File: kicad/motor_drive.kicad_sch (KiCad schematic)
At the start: 10 parts, among them U6 DRV8452DDWR

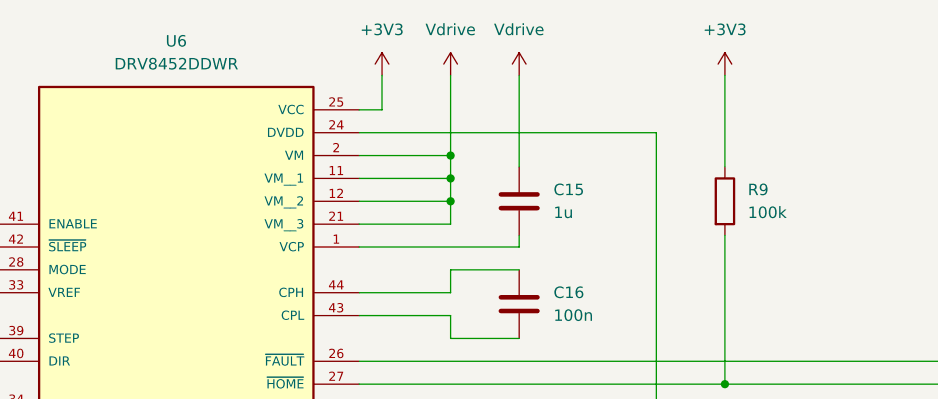
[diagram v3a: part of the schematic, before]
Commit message: Finished the schematic and started the PCB.
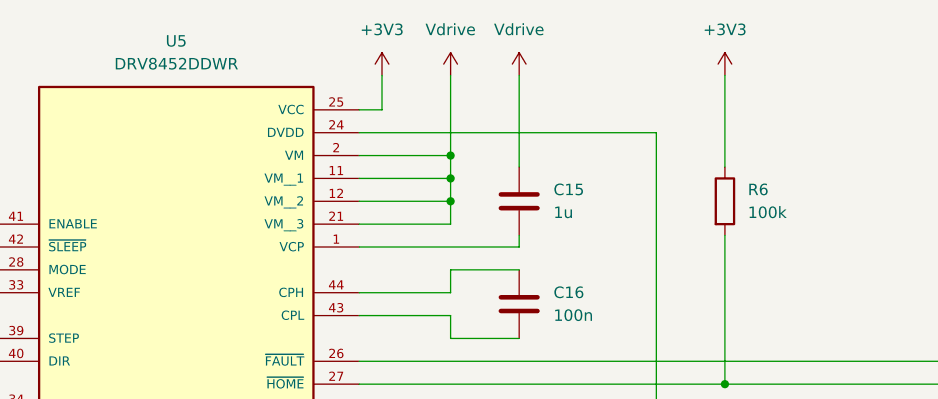
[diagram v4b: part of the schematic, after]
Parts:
- R6: renamed from R9; MF YAGEO -> Yageo
- renumbered U6 to U5
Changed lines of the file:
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@@
 		(dnp no)
 		(fields_autoplaced yes)
-		(property "Reference" "#PWR052"
+		(property "Reference" "#PWR046"
 			(at 160.02 157.48 0)
 			(effects
@@
 			(project ""
 				(path "/914c4b67-a7a4-47f3-8515-668040fd3f8c/e5516eed-629d-4c0b-bb03-2e43d030d802"
-					(reference "#PWR052")
+					(reference "#PWR046")
 					(unit 1)
 				)
@@
 		(dnp no)
 		(fields_autoplaced yes)
-		(property "Reference" "#PWR057"
+		(property "Reference" "#PWR051"
 			(at 231.14 157.48 0)
 			(effects
@@
 			(project "tv_slider"
 				(path "/914c4b67-a7a4-47f3-8515-668040fd3f8c/e5516eed-629d-4c0b-bb03-2e43d030d802"
-					(reference "#PWR057")
+					(reference "#PWR051")
 					(unit 1)
 				)
@@
 		(on_board yes)
 		(dnp no)
-		(property "Reference" "#PWR044"
+		(property "Reference" "#PWR038"
 			(at 175.26 50.8 0)
 			(effects
@@
 			(project "tv_slider"
 				(path "/914c4b67-a7a4-47f3-8515-668040fd3f8c/e5516eed-629d-4c0b-bb03-2e43d030d802"
-					(reference "#PWR044")
+					(reference "#PWR038")
 					(unit 1)
 				)
@@
 		(dnp no)
 		(fields_autoplaced yes)
-		(property "Reference" "#PWR041"
+		(property "Reference" "#PWR035"
 			(at 111.76 50.8 0)
 			(effects
@@
 			(project "tv_slider"
 				(path "/914c4b67-a7a4-47f3-8515-668040fd3f8c/e5516eed-629d-4c0b-bb03-2e43d030d802"
-					(reference "#PWR041")
+					(reference "#PWR035")
 					(unit 1)
 				)
@@
 		(dnp no)
 		(fields_autoplaced yes)
-		(property "Reference" "#PWR051"
+		(property "Reference" "#PWR045"
 			(at 111.76 157.48 0)
 			(effects
@@
 			(project "tv_slider"
 				(path "/914c4b67-a7a4-47f3-8515-668040fd3f8c/e5516eed-629d-4c0b-bb03-2e43d030d802"
-					(reference "#PWR051")
+					(reference "#PWR045")
 					(unit 1)
 				)
@@
 		(on_board yes)
 		(dnp no)
-		(property "Reference" "#PWR047"
+		(property "Reference" "#PWR041"
 			(at 204.47 142.24 0)
 			(effects
@@
 			(project "tv_slider"
 				(path "/914c4b67-a7a4-47f3-8515-668040fd3f8c/e5516eed-629d-4c0b-bb03-2e43d030d802"
-					(reference "#PWR047")
+					(reference "#PWR041")
 					(unit 1)
 				)
@@
 		(dnp no)
 		(fields_autoplaced yes)
-		(property "Reference" "R9"
+		(property "Reference" "R6"
 			(at 200.66 59.6899 0)
 			(effects
@@
 			)
 		)
-		(property "MF" "YAGEO"
+		(property "MF" "Yageo"
 			(at 198.12 60.96 0)
 			(effects
@@
 			(project "tv_slider"
 				(path "/914c4b67-a7a4-47f3-8515-668040fd3f8c/e5516eed-629d-4c0b-bb03-2e43d030d802"
-					(reference "R9")
+					(reference "R6")
 					(unit 1)
 				)
@@
 		(dnp no)
 		(fields_autoplaced yes)
-		(property "Reference" "#PWR055"
+		(property "Reference" "#PWR049"
 			(at 204.47 157.48 0)
 			(effects
@@
 			(project "tv_slider"
 				(path "/914c4b67-a7a4-47f3-8515-668040fd3f8c/e5516eed-629d-4c0b-bb03-2e43d030d802"
-					(reference "#PWR055")
+					(reference "#PWR049")
 					(unit 1)
 				)
@@
 		(dnp no)
 		(fields_autoplaced yes)
-		(property "Reference" "#PWR053"
+		(property "Reference" "#PWR047"
 			(at 175.26 157.48 0)
 			(effects
@@
 			(project "tv_slider"
 				(path "/914c4b67-a7a4-47f3-8515-668040fd3f8c/e5516eed-629d-4c0b-bb03-2e43d030d802"
-					(reference "#PWR053")
+					(reference "#PWR047")
 					(unit 1)
 				)
@@
 		(dnp no)
 		(fields_autoplaced yes)
-		(property "Reference" "#PWR042"
+		(property "Reference" "#PWR036"
 			(at 160.02 50.8 0)
 			(effects
@@
 			(project ""
 				(path "/914c4b67-a7a4-47f3-8515-668040fd3f8c/e5516eed-629d-4c0b-bb03-2e43d030d802"
-					(reference "#PWR042")
+					(reference "#PWR036")
 					(unit 1)
 				)
@@
 		(on_board yes)
 		(dnp no)
-		(property "Reference" "#PWR049"
+		(property "Reference" "#PWR043"
 			(at 231.14 142.24 0)
 			(effects
@@
 			(project "tv_slider"
 				(path "/914c4b67-a7a4-47f3-8515-668040fd3f8c/e5516eed-629d-4c0b-bb03-2e43d030d802"
-					(reference "#PWR049")
+					(reference "#PWR043")
 					(unit 1)
 				)
@@
 		(on_board yes)
 		(dnp no)
-		(property "Reference" "#PWR048"
+		(property "Reference" "#PWR042"
 			(at 217.17 142.24 0)
 			(effects
@@
 			(project "tv_slider"
 				(path "/914c4b67-a7a4-47f3-8515-668040fd3f8c/e5516eed-629d-4c0b-bb03-2e43d030d802"
-					(reference "#PWR048")
+					(reference "#PWR042")
 					(unit 1)
 				)
@@
 		(on_board yes)
 		(dnp no)
-		(property "Reference" "#PWR050"
+		(property "Reference" "#PWR044"
 			(at 245.11 142.24 0)
 			(effects
@@
 			(project "tv_slider"
 				(path "/914c4b67-a7a4-47f3-8515-668040fd3f8c/e5516eed-629d-4c0b-bb03-2e43d030d802"
-					(reference "#PWR050")
+					(reference "#PWR044")
 					(unit 1)
 				)
@@
 		(dnp no)
 		(fields_autoplaced yes)
-		(property "Reference" "#PWR045"
+		(property "Reference" "#PWR039"
 			(at 198.12 50.8 0)
 			(effects
@@
 			(project "tv_slider"
 				(path "/914c4b67-a7a4-47f3-8515-668040fd3f8c/e5516eed-629d-4c0b-bb03-2e43d030d802"
-					(reference "#PWR045")
+					(reference "#PWR039")
 					(unit 1)
 				)
@@
 		(dnp no)
 		(fields_autoplaced yes)
-		(property "Reference" "#PWR056"
+		(property "Reference" "#PWR050"
 			(at 217.17 157.48 0)
 			(effects
@@
 			(project "tv_slider"
 				(path "/914c4b67-a7a4-47f3-8515-668040fd3f8c/e5516eed-629d-4c0b-bb03-2e43d030d802"
-					(reference "#PWR056")
+					(reference "#PWR050")
 					(unit 1)
 				)
@@
 		(dnp no)
 		(fields_autoplaced yes)
-		(property "Reference" "#PWR054"
+		(property "Reference" "#PWR048"
 			(at 190.5 157.48 0)
 			(effects
@@
 			(project "tv_slider"
 				(path "/914c4b67-a7a4-47f3-8515-668040fd3f8c/e5516eed-629d-4c0b-bb03-2e43d030d802"
-					(reference "#PWR054")
+					(reference "#PWR048")
 					(unit 1)
 				)
@@
 		(on_board yes)
 		(dnp no)
-		(property "Reference" "#PWR043"
+		(property "Reference" "#PWR037"
 			(at 167.64 50.8 0)
 			(effects
@@
 			(project ""
 				(path "/914c4b67-a7a4-47f3-8515-668040fd3f8c/e5516eed-629d-4c0b-bb03-2e43d030d802"
-					(reference "#PWR043")
+					(reference "#PWR037")
 					(unit 1)
 				)
@@
 		(dnp no)
 		(fields_autoplaced yes)
-		(property "Reference" "#PWR046"
+		(property "Reference" "#PWR040"
 			(at 175.26 142.24 0)
 			(effects
@@
 			(project "tv_slider"
 				(path "/914c4b67-a7a4-47f3-8515-668040fd3f8c/e5516eed-629d-4c0b-bb03-2e43d030d802"
-					(reference "#PWR046")
+					(reference "#PWR040")
 					(unit 1)
 				)
@@
 		(dnp no)
 		(fields_autoplaced yes)
-		(property "Reference" "#PWR058"
+		(property "Reference" "#PWR052"
 			(at 245.11 157.48 0)
 			(effects
@@
 			(project "tv_slider"
 				(path "/914c4b67-a7a4-47f3-8515-668040fd3f8c/e5516eed-629d-4c0b-bb03-2e43d030d802"
-					(reference "#PWR058")
+					(reference "#PWR052")
 					(unit 1)
 				)
@@
 		(dnp no)
 		(fields_autoplaced yes)
-		(property "Reference" "U6"
+		(property "Reference" "U5"
 			(at 137.16 43.18 0)
 			(effects
@@
 			(project "tv_slider"
 				(path "/914c4b67-a7a4-47f3-8515-668040fd3f8c/e5516eed-629d-4c0b-bb03-2e43d030d802"
-					(reference "U6")
-					(unit 1)
-				)
+					(reference "U5")
+					(unit 1)
+				)

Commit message: Completed the PCB design. Ready for final review.
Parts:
- removed R6: 100k, Resistor_SMD:R_0603_1608Metric, symbol Device:R
- removed U5: DRV8452DDWR, local_library:IC_DRV8452DDWR, symbol local_library:DRV8452DDWR
- added U9: DRV8452SPWPR, local_library:IC_DRV8452SPWPR, symbol local_library:DRV8452SPWPR
- C21, C22: value 150u -> 100u; footprint Capacitor_SMD:CP_Elec_10x12.5 -> Capacitor_SMD:CP_Elec_8x11.9; MP A768MS157M1HLAE024 -> A768KS107M1HLAE030; SupplierPN 399-A768MS157M1HLAE024TR-ND -> 399-A768KS107M1HLAE030CT-ND
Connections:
- net +3V3: now also U9.19 (VCC)
- net A+: now also U9.4 (AOUT1), U9.5 (AOUT1__1)
- net A-: now also U9.6 (AOUT2), U9.7 (AOUT2__1)
- net B+: now also U9.10 (BOUT1), U9.11 (BOUT1__1)
- net B-: now also U9.8 (BOUT2), U9.9 (BOUT2__1)
- net DIR: now also U9.24 (DIR)
- net ENABLE: now also U9.25 (ENABLE)
- net GND: now also U9.12 (PGNDB), U9.14 (GND), U9.17 (VREF), U9.29 (PAD), U9.3 (PGNDA)
- net MISO: now also U9.20 (SDO)
- net MOSI: now also U9.21 (SDI)
- net SCLK: now also U9.22 (SCLK)
- net STEP: now also U9.23 (STEP)
- net Vdrive: now also U9.13 (VM__1), U9.2 (VM)
- net ~{CS}: now also U9.18 (~{SCS})
- net ~{FAULT}: now also U9.16 (~{FAULT})
- net ~{SLEEP}: now also U9.26 (~{SLEEP})
- net at C15.2: now also U9.1 (VCP)
- net at C18.1: now also U9.15 (DVDD)
- net at C16.2: now also U9.27 (CPL)
- net at C16.1: now also U9.28 (CPH)
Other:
- moved on the sheet: C15, C16, C17, C18, C19, C20, C22

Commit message: Reviewed the part numbers, footprints and pin numbers.
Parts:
- C21, C22: Dielectric Electrolytic -> (none)
- U9: MF (none) -> Texas Instruments; MP (none) -> DRV8452SPWPR; Supplier (none) -> Digi-Key; SupplierPN (none) -> 296-DRV8452SPWPRCT-ND
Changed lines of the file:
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@@
+			)
+		)
+		(property "MF" "Texas Instruments"
+			(at 137.16 73.66 0)
+			(effects
+				(font
+					(size 1.27 1.27)
+				)
+				(hide yes)
+			)
+		)
+		(property "MP" "DRV8452SPWPR"
+			(at 137.16 73.66 0)
+			(effects
+				(font
+					(size 1.27 1.27)
+				)
+				(hide yes)
+			)
+		)
+		(property "SNAPEDA_PN" ""
+			(at 137.16 73.66 0)
+			(effects
+				(font
+					(size 1.27 1.27)
+				)
+				(hide yes)
+			)
+		)
+		(property "Supplier" "Digi-Key"
+			(at 137.16 73.66 0)
+			(effects
+				(font
+					(size 1.27 1.27)
+				)
+				(hide yes)
+			)
+		)
+		(property "SupplierPN" "296-DRV8452SPWPRCT-ND"
+			(at 137.16 73.66 0)
+			(effects
+				(font
+					(size 1.27 1.27)
+				)
+				(hide yes)
 			)
 		)
@@
 			)
 		)
-		(property "Dielectric" "Electrolytic"
+		(property "Dielectric" ""
 			(at 232.41 116.84 0)
 			(effects
@@
 		)
 		(property "SupplierPN" "399-A768KS107M1HLAE030CT-ND"
+			(at 232.41 116.84 0)
+			(effects
+				(font
+					(size 1.27 1.27)
+				)
+				(hide yes)
+			)
+		)
+		(property "SNAPEDA_PN" ""
 			(at 232.41 116.84 0)
 			(effects
@@
 			)
 		)
+		(property "SNAPEDA_PN" ""
+			(at 175.26 50.8 0)
+			(effects
+				(font
+					(size 1.27 1.27)
+				)
+				(hide yes)
+			)
+		)
 		(pin "2"
 		)
@@
 		)
 		(property "SupplierPN" "490-3285-1-ND"
+			(at 176.53 116.84 0)
+			(effects
+				(font
+					(size 1.27 1.27)
+				)
+				(hide yes)
+			)
+		)
+		(property "SNAPEDA_PN" ""
 			(at 176.53 116.84 0)
 			(effects
@@
 			)
 		)
+		(property "SNAPEDA_PN" ""
+			(at 191.77 116.84 0)
+			(effects
+				(font
+					(size 1.27 1.27)
+				)
+				(hide yes)
+			)
+		)
 		(pin "2"
 		)
@@
 			)
 		)
+		(property "SNAPEDA_PN" ""
+			(at 205.74 116.84 0)
+			(effects
+				(font
+					(size 1.27 1.27)
+				)
+				(hide yes)
+			)
+		)
 		(pin "2"
 		)
@@
 			)
 		)
+		(property "SNAPEDA_PN" ""
+			(at 218.44 116.84 0)
+			(effects
+				(font
+					(size 1.27 1.27)
+				)
+				(hide yes)
+			)
+		)
 		(pin "2"
 		)
@@
 			)
 		)
-		(property "Dielectric" "Electrolytic"
+		(property "Dielectric" ""
 			(at 246.38 116.84 0)
 			(effects
@@
 		)
 		(property "SupplierPN" "399-A768KS107M1HLAE030CT-ND"
+			(at 246.38 116.84 0)
+			(effects
+				(font
+					(size 1.27 1.27)
+				)
+				(hide yes)
+			)
+		)
+		(property "SNAPEDA_PN" ""
 			(at 246.38 116.84 0)
 			(effects
@@
 			(at 175.26 62.23 0)
 			(effects
+				(font
+					(size 1.27 1.27)
+				)
+				(hide yes)
+			)
+		)
+		(property "SNAPEDA_PN" ""
+			(at 175.26 62.23 0)
+			(effects

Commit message: Re-annotated and added extra capacitors for the 5V and 3V3 DC-DC converters. Added testpoints to the electronic fuse.
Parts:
- renumbered C15 to C17, C16 to C18, C17 to C19, C18 to C20, C19 to C21, C20 to C22, C21 to C23, C22 to C24, U9 to U5
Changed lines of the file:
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@@
 		(dnp no)
 		(fields_autoplaced yes)
-		(property "Reference" "U9"
+		(property "Reference" "U5"
 			(at 137.16 38.1 0)
 			(effects
@@
 			(project ""
 				(path "/914c4b67-a7a4-47f3-8515-668040fd3f8c/e5516eed-629d-4c0b-bb03-2e43d030d802"
-					(reference "U9")
+					(reference "U5")
 					(unit 1)
 				)
@@
 		(dnp no)
 		(fields_autoplaced yes)
-		(property "Reference" "#PWR046"
+		(property "Reference" "#PWR048"
 			(at 161.29 129.54 0)
 			(effects
@@
 			(project ""
 				(path "/914c4b67-a7a4-47f3-8515-668040fd3f8c/e5516eed-629d-4c0b-bb03-2e43d030d802"
-					(reference "#PWR046")
+					(reference "#PWR048")
 					(unit 1)
 				)
@@
 		(dnp no)
 		(fields_autoplaced yes)
-		(property "Reference" "#PWR051"
+		(property "Reference" "#PWR053"
 			(at 232.41 129.54 0)
 			(effects
@@
 			(project "tv_slider"
 				(path "/914c4b67-a7a4-47f3-8515-668040fd3f8c/e5516eed-629d-4c0b-bb03-2e43d030d802"
-					(reference "#PWR051")
+					(reference "#PWR053")
 					(unit 1)
 				)
@@
 		(dnp no)
 		(fields_autoplaced yes)
-		(property "Reference" "C21"
+		(property "Reference" "C23"
 			(at 236.22 114.6809 0)
 			(effects
@@
 			(project "tv_slider"
 				(path "/914c4b67-a7a4-47f3-8515-668040fd3f8c/e5516eed-629d-4c0b-bb03-2e43d030d802"
-					(reference "C21")
+					(reference "C23")
 					(unit 1)
 				)
@@
 		(on_board yes)
 		(dnp no)
-		(property "Reference" "#PWR038"
+		(property "Reference" "#PWR041"
 			(at 175.26 44.45 0)
 			(effects
@@
 			(project "tv_slider"
 				(path "/914c4b67-a7a4-47f3-8515-668040fd3f8c/e5516eed-629d-4c0b-bb03-2e43d030d802"
-					(reference "#PWR038")
+					(reference "#PWR041")
 					(unit 1)
 				)
@@
 		(dnp no)
 		(fields_autoplaced yes)
-		(property "Reference" "#PWR045"
+		(property "Reference" "#PWR047"
 			(at 113.03 129.54 0)
 			(effects
@@
 			(project "tv_slider"
 				(path "/914c4b67-a7a4-47f3-8515-668040fd3f8c/e5516eed-629d-4c0b-bb03-2e43d030d802"
-					(reference "#PWR045")
+					(reference "#PWR047")
 					(unit 1)
 				)
@@
 		(on_board yes)
 		(dnp no)
-		(property "Reference" "#PWR041"
+		(property "Reference" "#PWR043"
 			(at 205.74 114.3 0)
 			(effects
@@
 			(project "tv_slider"
 				(path "/914c4b67-a7a4-47f3-8515-668040fd3f8c/e5516eed-629d-4c0b-bb03-2e43d030d802"
-					(reference "#PWR041")
+					(reference "#PWR043")
 					(unit 1)
 				)
@@
 		(dnp no)
 		(fields_autoplaced yes)
-		(property "Reference" "C15"
+		(property "Reference" "C17"
 			(at 179.07 49.5299 0)
 			(effects
@@
 			(project "tv_slider"
 				(path "/914c4b67-a7a4-47f3-8515-668040fd3f8c/e5516eed-629d-4c0b-bb03-2e43d030d802"
-					(reference "C15")
+					(reference "C17")
 					(unit 1)
 				)
@@
 		(on_board yes)
 		(dnp no)
-		(property "Reference" "C17"
+		(property "Reference" "C19"
 			(at 180.34 115.5699 0)
 			(effects
@@
 			(project "tv_slider"
 				(path "/914c4b67-a7a4-47f3-8515-668040fd3f8c/e5516eed-629d-4c0b-bb03-2e43d030d802"
-					(reference "C17")
+					(reference "C19")
 					(unit 1)
 				)
@@
 		(dnp no)
 		(fields_autoplaced yes)
-		(property "Reference" "#PWR049"
+		(property "Reference" "#PWR051"
 			(at 205.74 129.54 0)
 			(effects
@@
 			(project "tv_slider"
 				(path "/914c4b67-a7a4-47f3-8515-668040fd3f8c/e5516eed-629d-4c0b-bb03-2e43d030d802"
-					(reference "#PWR049")
+					(reference "#PWR051")
 					(unit 1)
 				)
@@
 		(dnp no)
 		(fields_autoplaced yes)
-		(property "Reference" "#PWR047"
+		(property "Reference" "#PWR049"
 			(at 176.53 129.54 0)
 			(effects
@@
 			(project "tv_slider"
 				(path "/914c4b67-a7a4-47f3-8515-668040fd3f8c/e5516eed-629d-4c0b-bb03-2e43d030d802"
-					(reference "#PWR047")
+					(reference "#PWR049")
 					(unit 1)
 				)
@@
 		(dnp no)
 		(fields_autoplaced yes)
-		(property "Reference" "C18"
+		(property "Reference" "C20"
 			(at 195.58 115.5699 0)
 			(effects
@@
 			(project ""
 				(path "/914c4b67-a7a4-47f3-8515-668040fd3f8c/e5516eed-629d-4c0b-bb03-2e43d030d802"
-					(reference "C18")
+					(reference "C20")
 					(unit 1)
 				)
@@
 		(dnp no)
 		(fields_autoplaced yes)
-		(property "Reference" "#PWR036"
+		(property "Reference" "#PWR039"
 			(at 160.02 44.45 0)
 			(effects
@@
 			(project ""
 				(path "/914c4b67-a7a4-47f3-8515-668040fd3f8c/e5516eed-629d-4c0b-bb03-2e43d030d802"
-					(reference "#PWR036")
+					(reference "#PWR039")
 					(unit 1)
 				)
@@
 		(on_board yes)
 		(dnp no)
-		(property "Reference" "#PWR043"
+		(property "Reference" "#PWR045"
 			(at 232.41 114.3 0)
 			(effects
@@
 			(project "tv_slider"
 				(path "/914c4b67-a7a4-47f3-8515-668040fd3f8c/e5516eed-629d-4c0b-bb03-2e43d030d802"
-					(reference "#PWR043")
+					(reference "#PWR045")
 					(unit 1)
 				)
@@
 		(on_board yes)
 		(dnp no)
-		(property "Reference" "#PWR042"
+		(property "Reference" "#PWR044"
 			(at 218.44 114.3 0)
 			(effects
@@
 			(project "tv_slider"
 				(path "/914c4b67-a7a4-47f3-8515-668040fd3f8c/e5516eed-629d-4c0b-bb03-2e43d030d802"
-					(reference "#PWR042")
+					(reference "#PWR044")
 					(unit 1)
 				)
@@
 		(on_board yes)
 		(dnp no)
-		(property "Reference" "#PWR044"
+		(property "Reference" "#PWR046"
 			(at 246.38 114.3 0)
 			(effects
@@
 			(project "tv_slider"
 				(path "/914c4b67-a7a4-47f3-8515-668040fd3f8c/e5516eed-629d-4c0b-bb03-2e43d030d802"
-					(reference "#PWR044")
+					(reference "#PWR046")
 					(unit 1)
 				)
@@
 		(dnp no)
 		(fields_autoplaced yes)
-		(property "Reference" "C19"
+		(property "Reference" "C21"
 			(at 209.55 115.5699 0)
 			(effects
@@
 			(project "tv_slider"
 				(path "/914c4b67-a7a4-47f3-8515-668040fd3f8c/e5516eed-629d-4c0b-bb03-2e43d030d802"
-					(reference "C19")
+					(reference "C21")
 					(unit 1)
 				)
@@
 		(dnp no)
 		(fields_autoplaced yes)
-		(property "Reference" "C20"
+		(property "Reference" "C22"
 			(at 222.25 115.5699 0)
 			(effects
@@
 			(project "tv_slider"
 				(path "/914c4b67-a7a4-47f3-8515-668040fd3f8c/e5516eed-629d-4c0b-bb03-2e43d030d802"
-					(reference "C20")
+					(reference "C22")
 					(unit 1)
 				)
@@
 		(dnp no)
 		(fields_autoplaced yes)
-		(property "Reference" "#PWR050"
+		(property "Reference" "#PWR052"
 			(at 218.44 129.54 0)
 			(effects
@@
 			(project "tv_slider"
 				(path "/914c4b67-a7a4-47f3-8515-668040fd3f8c/e5516eed-629d-4c0b-bb03-2e43d030d802"
-					(reference "#PWR050")
+					(reference "#PWR052")
 					(unit 1)
 				)
@@
 		(dnp no)
 		(fields_autoplaced yes)
-		(property "Reference" "#PWR048"
+		(property "Reference" "#PWR050"
 			(at 191.77 129.54 0)
 			(effects
@@
 			(project "tv_slider"
 				(path "/914c4b67-a7a4-47f3-8515-668040fd3f8c/e5516eed-629d-4c0b-bb03-2e43d030d802"
-					(reference "#PWR048")
+					(reference "#PWR050")
 					(unit 1)
 				)
@@
 		(on_board yes)
 		(dnp no)
-		(property "Reference" "#PWR037"
+		(property "Reference" "#PWR040"
 			(at 167.64 44.45 0)
 			(effects
@@
 			(project ""
 				(path "/914c4b67-a7a4-47f3-8515-668040fd3f8c/e5516eed-629d-4c0b-bb03-2e43d030d802"
-					(reference "#PWR037")
+					(reference "#PWR040")
 					(unit 1)
 				)
@@
 		(dnp no)
 		(fields_autoplaced yes)
-		(property "Reference" "C22"
+		(property "Reference" "C24"
 			(at 250.19 114.6809 0)
 			(effects
@@
 			(project "tv_slider"
 				(path "/914c4b67-a7a4-47f3-8515-668040fd3f8c/e5516eed-629d-4c0b-bb03-2e43d030d802"
-					(reference "C22")
+					(reference "C24")
 					(unit 1)
 				)
@@
 		(dnp no)
 		(fields_autoplaced yes)
-		(property "Reference" "#PWR040"
+		(property "Reference" "#PWR042"
 			(at 176.53 114.3 0)
 			(effects
@@
 			(project "tv_slider"
 				(path "/914c4b67-a7a4-47f3-8515-668040fd3f8c/e5516eed-629d-4c0b-bb03-2e43d030d802"
-					(reference "#PWR040")
+					(reference "#PWR042")
 					(unit 1)
 				)
@@
 		(dnp no)
 		(fields_autoplaced yes)
-		(property "Reference" "#PWR052"
+		(property "Reference" "#PWR054"
 			(at 246.38 129.54 0)
 			(effects
@@
 			(project "tv_slider"
 				(path "/914c4b67-a7a4-47f3-8515-668040fd3f8c/e5516eed-629d-4c0b-bb03-2e43d030d802"
-					(reference "#PWR052")
+					(reference "#PWR054")
 					(unit 1)
 				)
@@
 		(on_board yes)
 		(dnp no)
-		(property "Reference" "C16"
+		(property "Reference" "C18"
 			(at 179.07 60.9599 0)
 			(effects
@@
 			(project "tv_slider"
 				(path "/914c4b67-a7a4-47f3-8515-668040fd3f8c/e5516eed-629d-4c0b-bb03-2e43d030d802"
-					(reference "C16")
-					(unit 1)
-				)
+					(reference "C18")
+					(unit 1)
+				)

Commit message: Fixed up or explained all DRC violations.
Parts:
- added R10: 10k, Resistor_SMD:R_0603_1608Metric, symbol Device:R
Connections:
- net +3V3: now also R10.2
- net GND: no longer U5.17 (VREF)
- net ~{FAULT}: now also R10.1
